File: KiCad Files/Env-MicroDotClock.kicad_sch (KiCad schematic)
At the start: 40 parts, among them IC1 IS31FL3730-QFLS2-TR, IC2 IS31FL3730-QFLS2-TR, IC3 IS31FL3730-QFLS2-TR, IC4 IS31FL3730-QFLS2-TR, M1 Dip-14 Socket, M2 Dip-14 Socket, M3 Dip-14 Socket, M4 Dip-14 Socket, M5 Dip-14 Socket, M6 Dip-14 Socket, M7 Dip-14 Socket, M8 Dip-14 Socket, Q1 2SC1815, SW1 SKRK, SW2 SKRK, SW3 SKRK, SW4 SKRK, SW5 DIP SPST W5.08mm_P1.27mm, U1 Raspberry Pi Pico, U3 DS3231M

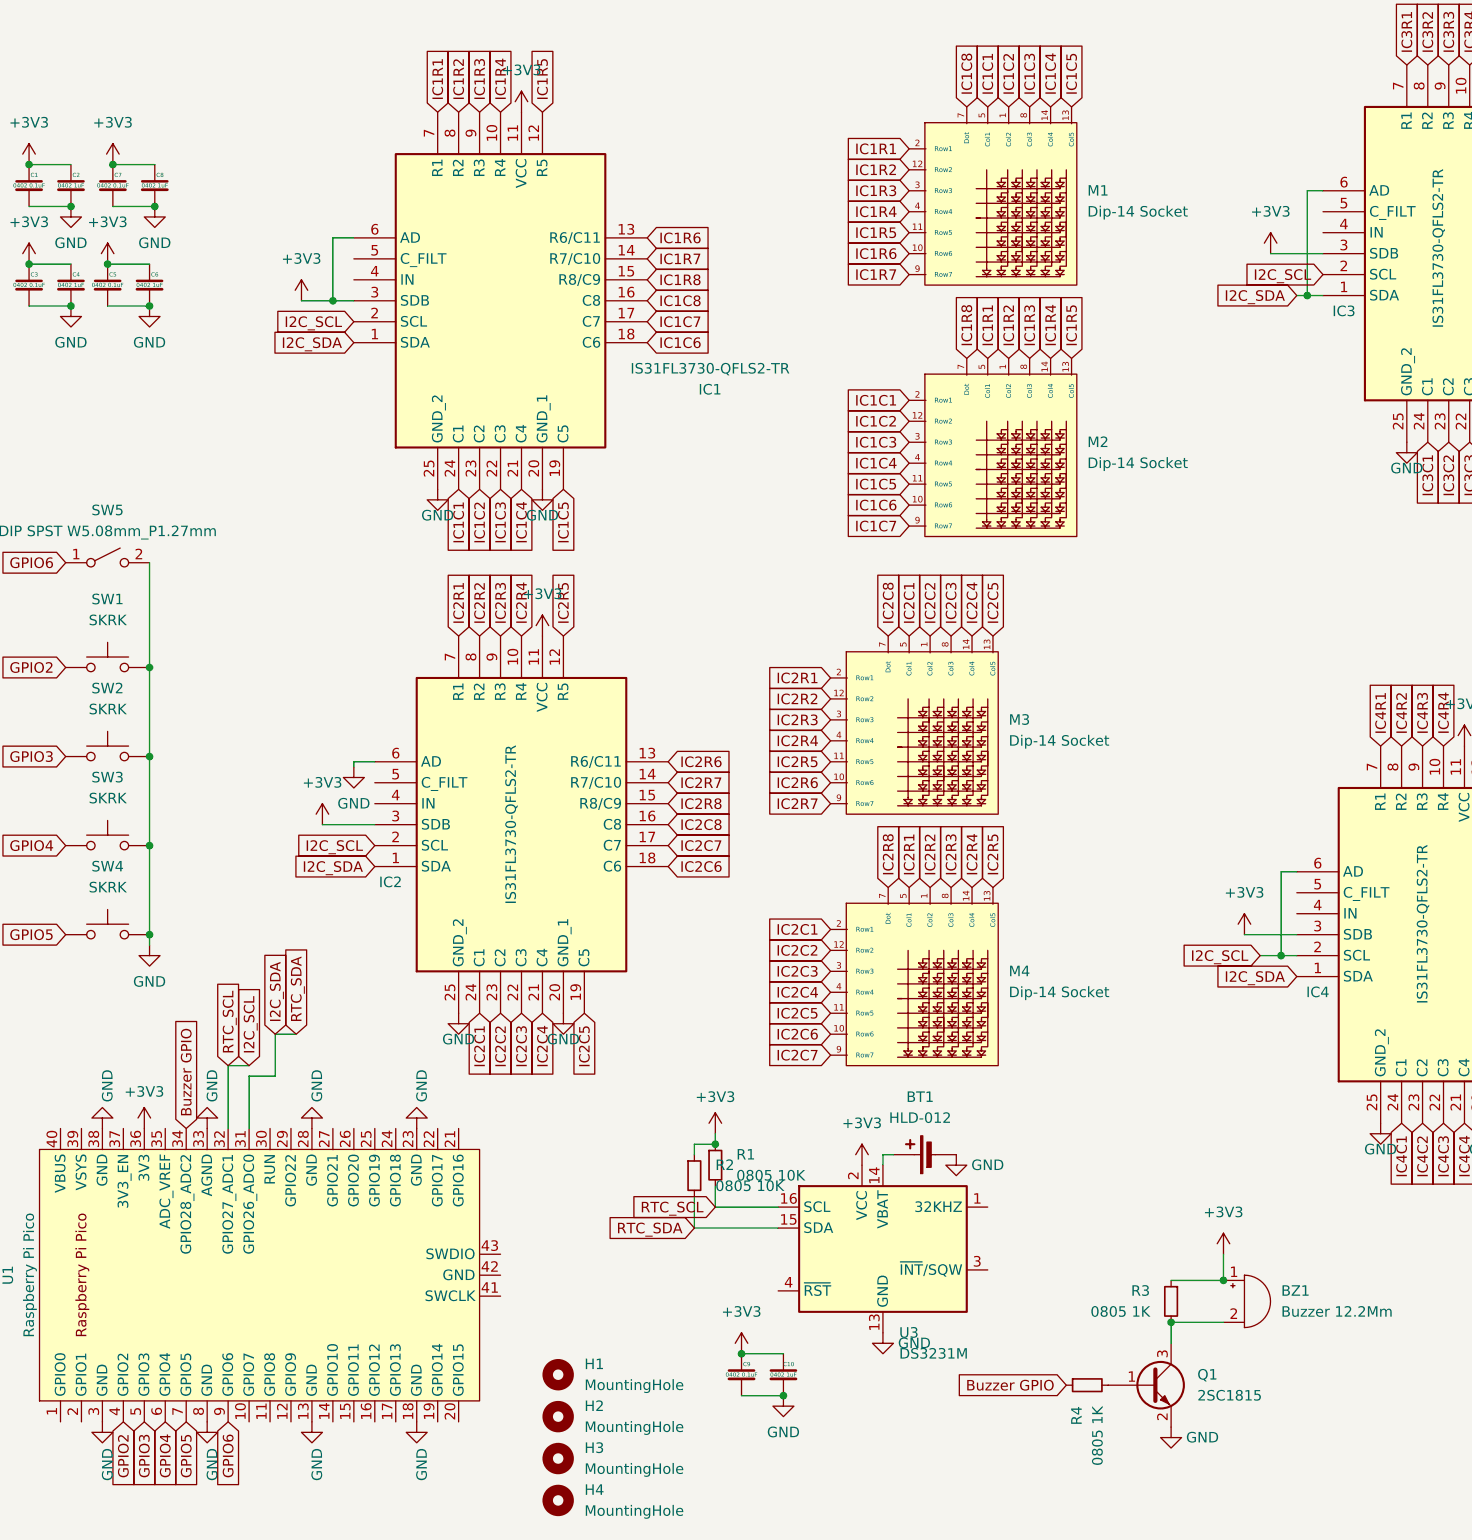
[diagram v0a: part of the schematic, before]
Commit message: moved all i2c devices to dedicated gpio pairs, added individual pullups, ensured everything is 3.3V VCC or logic level 3V3 tied
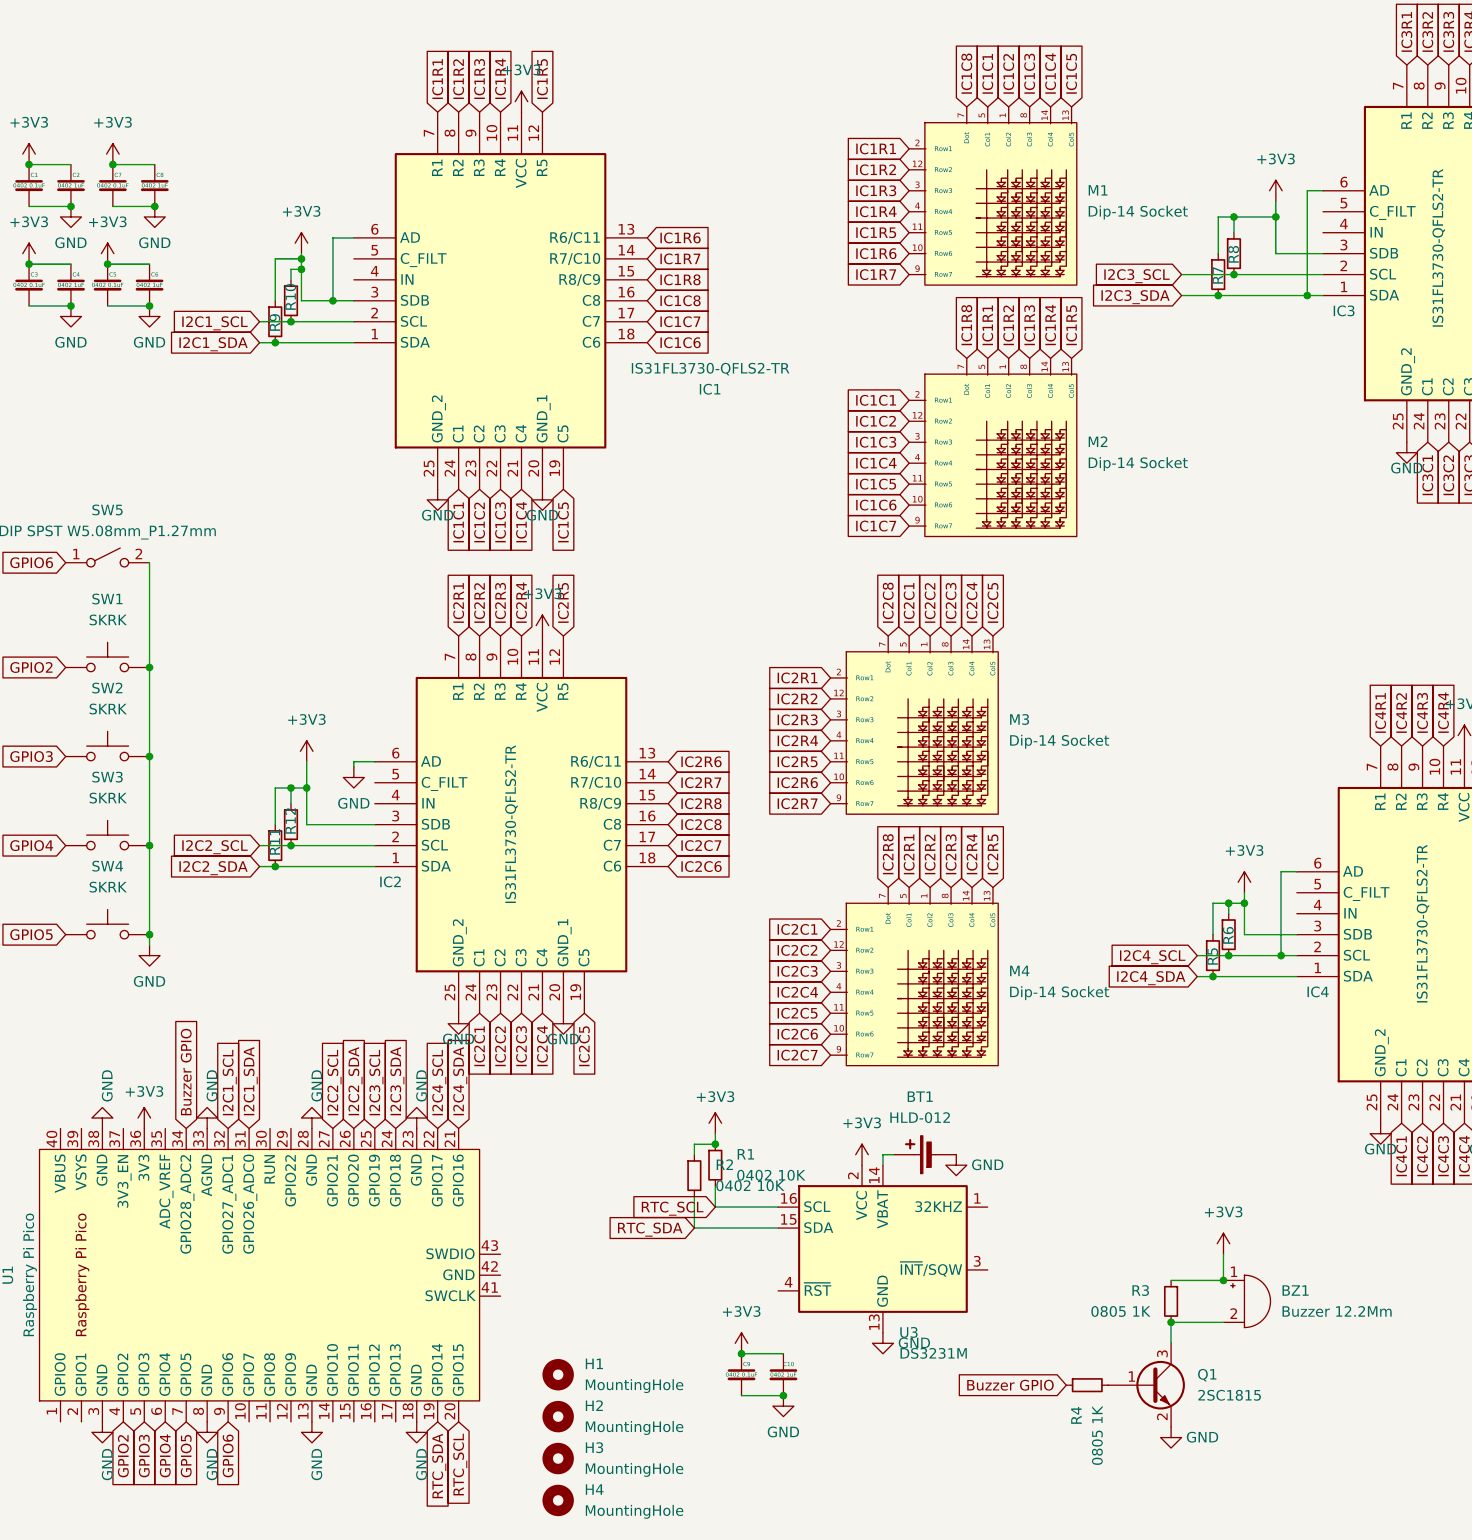
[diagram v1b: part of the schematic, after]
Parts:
- added R10, R11, R12, R5, R6, R7, R8, R9: 0402 10K, Resistor_SMD:R_0402_1005Metric, symbol Device:R_Small
- R1, R2: value 0805 10K -> 0402 10K; footprint Resistor_SMD:R_0805_2012Metric -> Resistor_SMD:R_0402_1005Metric
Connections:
- net +3V3: now also R10.1, R11.1, R12.1, R5.1, R6.1, R7.1, R8.1, R9.1
- net RTC_SDA: now reaches U1.19 (GPIO14)
- net RTC_SDA: now also R2.2, U3.15 (SDA)
- net RTC_SCL: now reaches U1.20 (GPIO15)
- net RTC_SCL: now also R1.2, U3.16 (SCL)
- net I2C4_SDA: now reaches U1.21 (GPIO16)
- net I2C4_SDA: now also IC4.1 (SDA), R5.2
- net I2C4_SCL: now reaches U1.22 (GPIO17)
- net I2C4_SCL: now also IC4.2 (SCL), IC4.6 (AD), R6.2
- net I2C3_SDA: now reaches U1.24 (GPIO18)
- net I2C3_SDA: now also IC3.1 (SDA), IC3.6 (AD), R7.2
- net I2C3_SCL: now reaches U1.25 (GPIO19)
- net I2C3_SCL: now also IC3.2 (SCL), R8.2
- net I2C2_SDA: now reaches U1.26 (GPIO20)
- net I2C2_SDA: now also IC2.1 (SDA), R11.2
- net I2C2_SCL: now reaches U1.27 (GPIO21)
- net I2C2_SCL: now also IC2.2 (SCL), R12.2
- removed net I2C_SCL: IC1.2 (SCL), IC2.2 (SCL), IC3.2 (SCL), IC4.2 (SCL), IC4.6 (AD), R1.2, U1.32 (GPIO27_ADC1), U3.16 (SCL)
- removed net I2C_SDA: IC1.1 (SDA), IC2.1 (SDA), IC3.1 (SDA), IC3.6 (AD), IC4.1 (SDA), R2.2, U1.31 (GPIO26_ADC0), U3.15 (SDA)
- new net I2C1_SCL: IC1.2 (SCL), R10.2, U1.32 (GPIO27_ADC1)
- new net I2C1_SDA: IC1.1 (SDA), R9.2, U1.31 (GPIO26_ADC0)

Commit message: changes toward a V2, replaced battery holder with larger one, moved rtc leftward to make space for larger battery.
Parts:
- BT1: value HLD-012 -> Keystone 3034; footprint Battery:BatteryHolder_LINX_BAT-HLD-012-SMT -> Battery:BatteryHolder_Keystone_3034_1x20mm
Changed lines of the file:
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@@
       (effects (font (size 1.27 1.27)))
     )
-    (property "Value" "HLD-012" (at 126.4285 149.225 90)
+    (property "Value" "Keystone 3034" (at 126.4285 149.225 90)
       (effects (font (size 1.27 1.27)))
     )
-    (property "Footprint" "Battery:BatteryHolder_LINX_BAT-HLD-012-SMT" (at 126.746 153.67 90)
+    (property "Footprint" "Battery:BatteryHolder_Keystone_3034_1x20mm" (at 126.746 153.67 90)
       (effects (font (size 1.27 1.27)) hide)
     )

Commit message: removed all traces for work on future version
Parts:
- removed SW5: DIP SPST W5.08mm_P1.27mm, Button_Switch_SMD:SW_DIP_SPSTx01_Slide_Copal_CHS-01A_W5.08mm_P1.27mm_JPin, symbol Switch:SW_SPST
- IC1, IC2, IC3, IC4: footprint Package_DFN_QFN:QFN-24-1EP_4x4mm_P0.5mm_EP2.6x2.6mm -> Package_DFN_QFN:QFN-24-1EP_4x4mm_P0.5mm_EP2.6x2.6mm_ThermalVias
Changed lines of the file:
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@@
   (junction (at 169.545 40.005) (diameter 0) (color 0 0 0 0)
   )
-  (junction (at 33.02 94.615) (diameter 0) (color 0 0 0 0)
-  )
   (junction (at 162.56 49.53) (diameter 0) (color 0 0 0 0)
   )
@@
     (stroke (width 0) (type default))
   )
-  (wire (pts (xy 33.02 81.915) (xy 33.02 94.615))
-    (stroke (width 0) (type default))
-  )
   (wire (pts (xy 170.18 119.38) (xy 172.085 119.38))
     (stroke (width 0) (type default))
@@
     )
   )
-  (global_label "GPIO6" (shape input) (at 22.86 81.915 180) (fields_autoplaced)
-    (effects (font (size 1.27 1.27)) (justify right))
-    (property "Intersheetrefs" "${INTERSHEET_REFS}" (at 14.2694 81.915 0)
-      (effects (font (size 1.27 1.27)) (justify right) hide)
-    )
-  )
   (global_label "IC4C7" (shape input) (at 239.395 154.305 180) (fields_autoplaced)
     (effects (font (size 1.27 1.27)) (justify right))
@@
       (effects (font (size 1.27 1.27)))
     )
-    (property "Footprint" "Package_DFN_QFN:QFN-24-1EP_4x4mm_P0.5mm_EP2.6x2.6mm" (at 203.835 47.32 0)
+    (property "Footprint" "Package_DFN_QFN:QFN-24-1EP_4x4mm_P0.5mm_EP2.6x2.6mm_ThermalVias" (at 203.835 47.32 0)
       (effects (font (size 1.27 1.27)) (justify left top) hide)
     )
@@
       (effects (font (size 1.27 1.27)))
     )
-    (property "Footprint" "Package_DFN_QFN:QFN-24-1EP_4x4mm_P0.5mm_EP2.6x2.6mm" (at 89.535 -29.515 0)
+    (property "Footprint" "Package_DFN_QFN:QFN-24-1EP_4x4mm_P0.5mm_EP2.6x2.6mm_ThermalVias" (at 89.535 -29.515 0)
       (effects (font (size 1.27 1.27)) (justify left top) hide)
     )
@@
     )
   )
-  (symbol (lib_id "Switch:SW_SPST") (at 27.94 81.915 0) (unit 1)
-    (in_bom yes) (on_board yes) (dnp no) (fields_autoplaced)
-    (property "Reference" "SW5" (at 27.94 75.565 0)
-      (effects (font (size 1.27 1.27)))
-    )
-    (property "Value" "DIP SPST W5.08mm_P1.27mm" (at 27.94 78.105 0)
-      (effects (font (size 1.27 1.27)))
-    )
-    (property "Footprint" "Button_Switch_SMD:SW_DIP_SPSTx01_Slide_Copal_CHS-01A_W5.08mm_P1.27mm_JPin" (at 27.94 81.915 0)
-      (effects (font (size 1.27 1.27)) hide)
-    )
-    (property "Datasheet" "~" (at 27.94 81.915 0)
-      (effects (font (size 1.27 1.27)) hide)
-    )
-    (pin "1")
-    (pin "2")
-    (instances
-      (project "Env-MicroDotClock"
-        (path "/3dbeb8d8-208e-4f6d-8d30-b14372f68a4f"
-          (reference "SW5") (unit 1)
-        )
-      )
-    )
-  )
   (symbol (lib_id "power:+3V3") (at 27.94 45.72 0) (unit 1)
     (in_bom yes) (on_board yes) (dnp no) (fields_autoplaced)
@@
       (effects (font (size 1.27 1.27)))
     )
-    (property "Footprint" "Package_DFN_QFN:QFN-24-1EP_4x4mm_P0.5mm_EP2.6x2.6mm" (at 207.01 -35.23 0)
+    (property "Footprint" "Package_DFN_QFN:QFN-24-1EP_4x4mm_P0.5mm_EP2.6x2.6mm_ThermalVias" (at 207.01 -35.23 0)
       (effects (font (size 1.27 1.27)) (justify left top) hide)
     )
@@
       (effects (font (size 1.27 1.27)))
     )
-    (property "Footprint" "Package_DFN_QFN:QFN-24-1EP_4x4mm_P0.5mm_EP2.6x2.6mm" (at 92.075 33.985 0)
+    (property "Footprint" "Package_DFN_QFN:QFN-24-1EP_4x4mm_P0.5mm_EP2.6x2.6mm_ThermalVias" (at 92.075 33.985 0)
       (effects (font (size 1.27 1.27)) (justify left top) hide)
     )

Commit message: schema push
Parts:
- added J1: Conn_01x06_Pin, Connector_PinHeader_2.54mm:PinHeader_1x06_P2.54mm_Vertical, symbol Connector:Conn_01x06_Pin
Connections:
- net GND: now also U1.42 (GND), J1.2 (Pin_2), J1.5 (Pin_5)
- net TX: now reaches U1.1 (GPIO0)
- net TX: now also J1.3 (Pin_3)
- net RX: now reaches U1.2 (GPIO1)
- net RX: now also J1.1 (Pin_1)
- net SWCLK: now reaches U1.41 (SWCLK)
- net SWCLK: now also J1.4 (Pin_4)
- net SWDIO: now reaches U1.43 (SWDIO)
- net SWDIO: now also J1.6 (Pin_6)
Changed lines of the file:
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@@
     (stroke (width 0) (type default))
   )
+  (wire (pts (xy 222.885 88.265) (xy 222.885 83.82))
+    (stroke (width 0) (type default))
+  )
   (wire (pts (xy 48.26 50.165) (xy 48.26 45.085))
     (stroke (width 0) (type default))
@@
     )
   )
+  (global_label "RX" (shape input) (at 225.425 83.82 270) (fields_autoplaced)
+    (effects (font (size 1.27 1.27)) (justify right))
+    (property "Intersheetrefs" "${INTERSHEET_REFS}" (at 225.425 89.2847 90)
+      (effects (font (size 1.27 1.27)) (justify right) hide)
+    )
+  )
   (global_label "IC2R2" (shape input) (at 115.57 98.425 180) (fields_autoplaced)
     (effects (font (size 1.27 1.27)) (justify right))
@@
     )
   )
+  (global_label "SWCLK" (shape input) (at 217.805 83.82 270) (fields_autoplaced)
+    (effects (font (size 1.27 1.27)) (justify right))
+    (property "Intersheetrefs" "${INTERSHEET_REFS}" (at 217.805 93.0342 90)
+      (effects (font (size 1.27 1.27)) (justify right) hide)
+    )
+  )
   (global_label "IC2C3" (shape input) (at 130.175 90.805 90) (fields_autoplaced)
     (effects (font (size 1.27 1.27)) (justify left))
@@
     )
   )
+  (global_label "SWDIO" (shape input) (at 212.725 83.82 270) (fields_autoplaced)
+    (effects (font (size 1.27 1.27)) (justify right))
+    (property "Intersheetrefs" "${INTERSHEET_REFS}" (at 212.725 92.6714 90)
+      (effects (font (size 1.27 1.27)) (justify right) hide)
+    )
+  )
+  (global_label "GND" (shape input) (at 75.565 168.275 0) (fields_autoplaced)
+    (effects (font (size 1.27 1.27)) (justify left))
+    (property "Intersheetrefs" "${INTERSHEET_REFS}" (at 82.4207 168.275 0)
+      (effects (font (size 1.27 1.27)) (justify left) hide)
+    )
+  )
   (global_label "IC1C1" (shape input) (at 134.62 26.67 90) (fields_autoplaced)
     (effects (font (size 1.27 1.27)) (justify left))
@@
     )
   )
+  (global_label "SWCLK" (shape input) (at 75.565 170.815 0) (fields_autoplaced)
+    (effects (font (size 1.27 1.27)) (justify left))
+    (property "Intersheetrefs" "${INTERSHEET_REFS}" (at 84.7792 170.815 0)
+      (effects (font (size 1.27 1.27)) (justify left) hide)
+    )
+  )
   (global_label "IC4R7" (shape input) (at 207.645 121.92 0) (fields_autoplaced)
     (effects (font (size 1.27 1.27)) (justify left))
@@
     )
   )
+  (global_label "TX" (shape input) (at 220.345 83.82 270) (fields_autoplaced)
+    (effects (font (size 1.27 1.27)) (justify right))
+    (property "Intersheetrefs" "${INTERSHEET_REFS}" (at 220.345 88.9823 90)
+      (effects (font (size 1.27 1.27)) (justify right) hide)
+    )
+  )
   (global_label "IC2R3" (shape input) (at 115.57 100.965 180) (fields_autoplaced)
     (effects (font (size 1.27 1.27)) (justify right))
@@
     )
   )
+  (global_label "RX" (shape input) (at 24.765 186.055 270) (fields_autoplaced)
+    (effects (font (size 1.27 1.27)) (justify right))
+    (property "Intersheetrefs" "${INTERSHEET_REFS}" (at 24.765 191.5197 90)
+      (effects (font (size 1.27 1.27)) (justify right) hide)
+    )
+  )
   (global_label "I2C2_SDA" (shape input) (at 46.355 118.745 180) (fields_autoplaced)
     (effects (font (size 1.27 1.27)) (justify right))
@@
     )
   )
+  (global_label "GND" (shape input) (at 215.265 83.82 270) (fields_autoplaced)
+    (effects (font (size 1.27 1.27)) (justify right))
+    (property "Intersheetrefs" "${INTERSHEET_REFS}" (at 215.265 90.6757 90)
+      (effects (font (size 1.27 1.27)) (justify right) hide)
+    )
+  )
   (global_label "IC3R1" (shape input) (at 252.095 51.435 90) (fields_autoplaced)
     (effects (font (size 1.27 1.27)) (justify left))
@@
     )
   )
+  (global_label "TX" (shape input) (at 22.225 186.055 270) (fields_autoplaced)
+    (effects (font (size 1.27 1.27)) (justify right))
+    (property "Intersheetrefs" "${INTERSHEET_REFS}" (at 22.225 191.2173 90)
+      (effects (font (size 1.27 1.27)) (justify right) hide)
+    )
+  )
   (global_label "I2C3_SDA" (shape input) (at 62.865 150.495 90) (fields_autoplaced)
     (effects (font (size 1.27 1.27)) (justify left))
@@
     )
   )
+  (global_label "SWDIO" (shape input) (at 75.565 165.735 0) (fields_autoplaced)
+    (effects (font (size 1.27 1.27)) (justify left))
+    (property "Intersheetrefs" "${INTERSHEET_REFS}" (at 84.4164 165.735 0)
+      (effects (font (size 1.27 1.27)) (justify left) hide)
+    )
+  )
   (global_label "IC2R6" (shape input) (at 95.885 106.045 0) (fields_autoplaced)
     (effects (font (size 1.27 1.27)) (justify left))
@@
     )
   )
+  (symbol (lib_id "power:GND") (at 222.885 88.265 0) (mirror y) (unit 1)
+    (in_bom yes) (on_board yes) (dnp no) (fields_autoplaced)
+    (property "Reference" "#PWR026" (at 222.885 94.615 0)
+      (effects (font (size 1.27 1.27)) hide)
+    )
+    (property "Value" "GND" (at 222.885 93.345 0)
+      (effects (font (size 1.27 1.27)))
+    )
+    (property "Footprint" "" (at 222.885 88.265 0)
+      (effects (font (size 1.27 1.27)) hide)
+    )
+    (property "Datasheet" "" (at 222.885 88.265 0)
+      (effects (font (size 1.27 1.27)) hide)
+    )
+    (pin "1")
+    (instances
+      (project "Env-MicroDotClock"
+        (path "/3dbeb8d8-208e-4f6d-8d30-b14372f68a4f"
+          (reference "#PWR026") (unit 1)
+        )
+      )
+    )
+  )
   (symbol (lib_id "power:GND") (at 198.12 67.31 0) (mirror y) (unit 1)
     (in_bom yes) (on_board yes) (dnp no) (fields_autoplaced)
@@
         )
       )
+    )
+  )
+  (symbol (lib_id "Connector:Conn_01x06_Pin") (at 220.345 78.74 270) (unit 1)
+    (in_bom yes) (on_board yes) (dnp no) (fields_autoplaced)
+    (property "Reference" "J1" (at 219.075 73.66 90)
+      (effects (font (size 1.27 1.27)))
+    )
+    (property "Value" "Conn_01x06_Pin" (at 219.075 76.2 90)
+      (effects (font (size 1.27 1.27)))
+    )
+    (property "Footprint" "Connector_PinHeader_2.54mm:PinHeader_1x06_P2.54mm_Vertical" (at 220.345 78.74 0)
+      (effects (font (size 1.27 1.27)) hide)
+    )
+    (property "Datasheet" "~" (at 220.345 78.74 0)
+      (effects (font (size 1.27 1.27)) hide)
+    )
+    (pin "1")
+    (pin "2")
+    (pin "3")
+    (pin "4")
+    (pin "5")
+    (pin "6")
+    (instances
+      (project "Env-MicroDotClock"
+        (path "/3dbeb8d8-208e-4f6d-8d30-b14372f68a4f"
+          (reference "J1") (unit 1)
+        )
+      )

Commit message: prettied up pcb some more and organised schematic
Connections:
- net GND: no longer J1.5 (Pin_5), U1.42 (GND)
- new net DEBUG-GND: J1.5 (Pin_5), U1.42 (GND)
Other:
- note added: "DISPLAYS AND ICs"
- note added: "MCU, RTC and related Circuitry"
- moved on the sheet: BT1, BZ1, C1, C10, C2, C3, C4, C5, C6, C7, C8, C9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
